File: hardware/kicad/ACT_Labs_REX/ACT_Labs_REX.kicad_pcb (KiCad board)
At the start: 2 copper layers, 138.8 x 120 mm, 40 parts, among them J1 PS1_Connector1, J2 JP1 Autofire, J3 JP3 Palanca Direccional, J4 JP4 Botones Frontales, J5 JP5 Botones laterales, J6 JP6 Autofire, SW1 SW_SPDT, SW10 SW_SPDT, SW2 SW_SPDT, SW3 SW_SPDT, SW4 SW_SPDT, SW5 SW_SPDT, SW6 SW_SPDT, SW7 SW_SPDT, SW8 SW_SPDT, SW9 SW_SPDT, U2 LD1117S33TR_SOT223

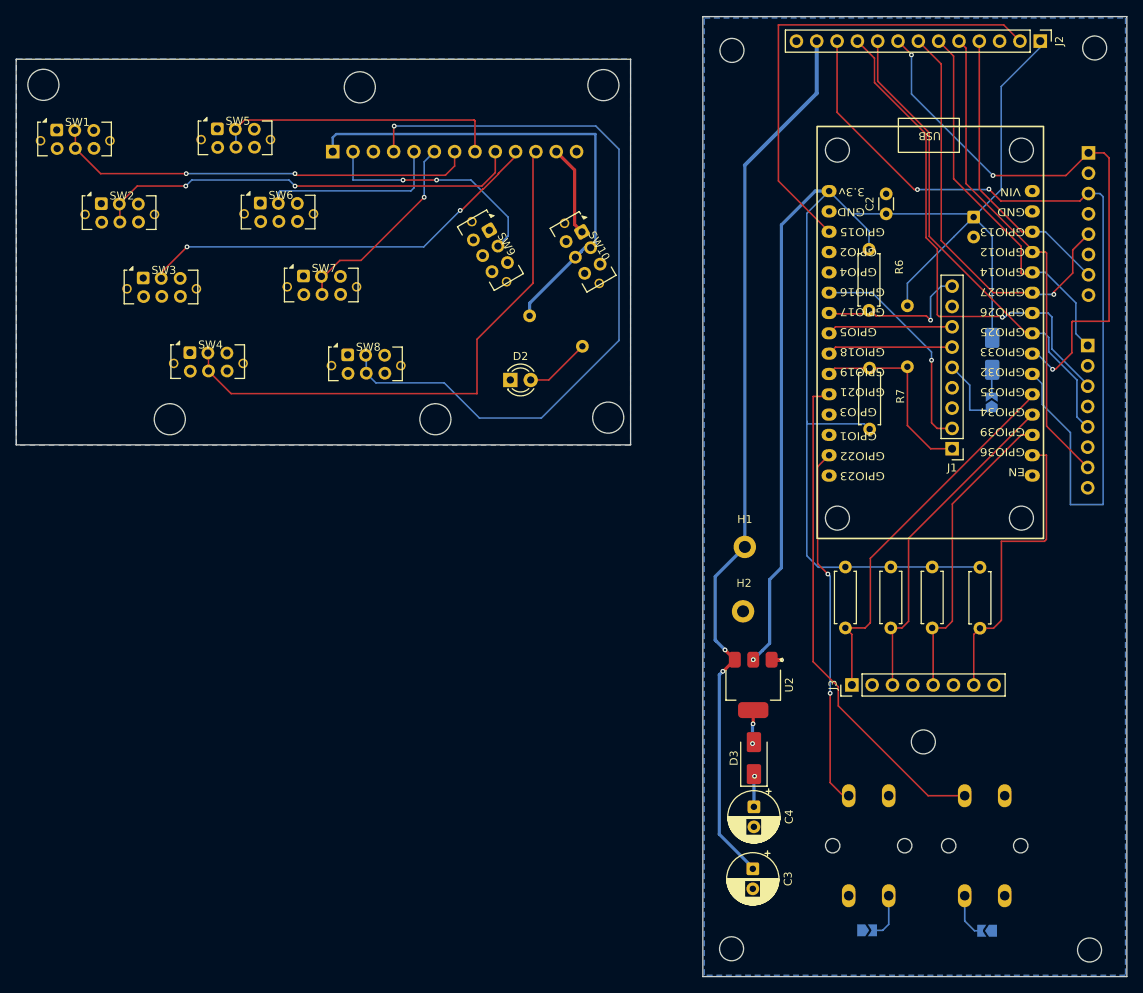
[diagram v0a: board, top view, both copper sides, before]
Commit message: hardware: update ACT Labs REX KiCad sources and gerbers
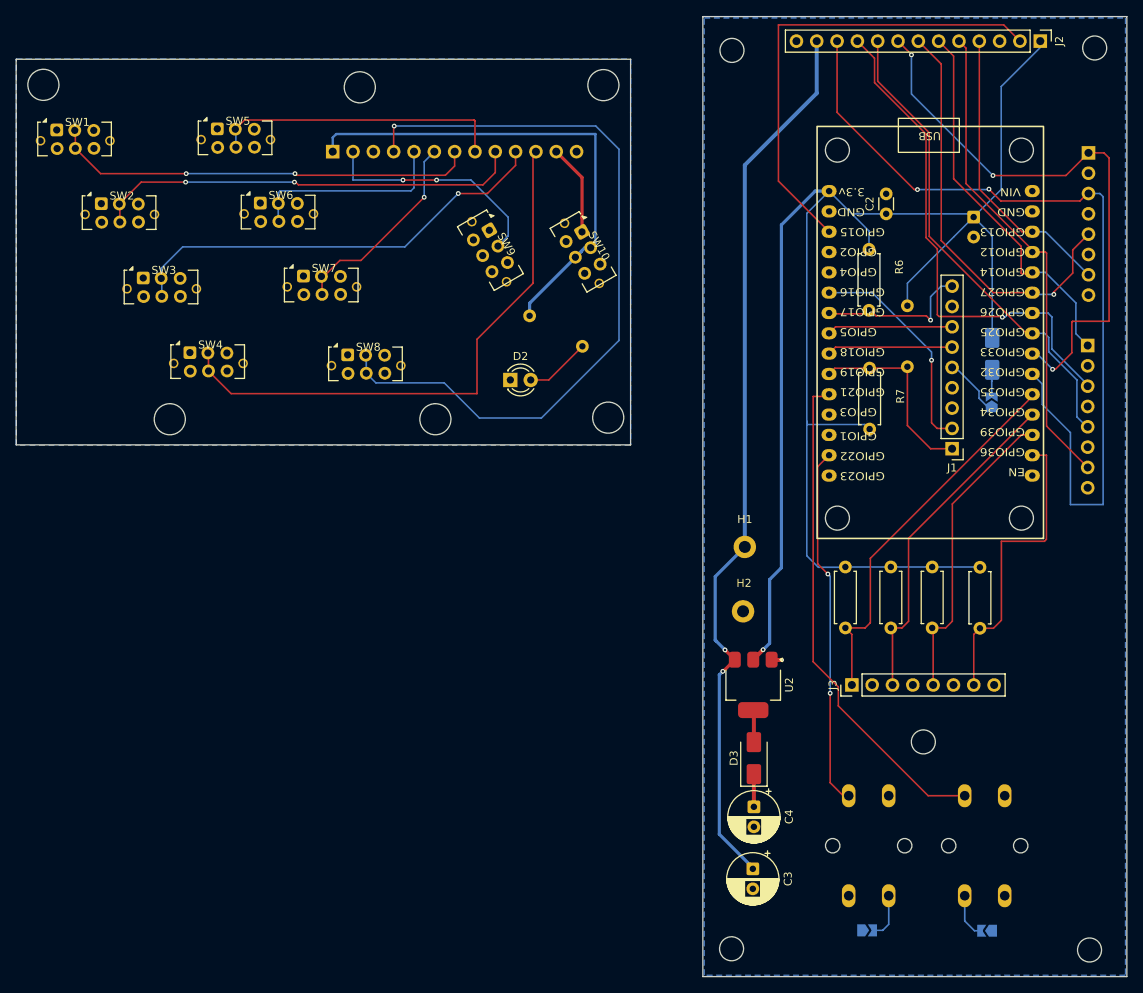
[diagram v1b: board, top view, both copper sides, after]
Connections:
- Select1 pad 1: //GND -> (no net)
- Select1 pad 2: //GND -> (no net)
- Start1 pad 2: //GND -> (no net)
- Start1 pad 3: //GND -> (no net)
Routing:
- net //AutoFire/AF_CIRCULO: track 51.8 -> 55.7 mm, vias 2 -> 1
- net //AutoFire/AF_CUADRADO: track 23.2 -> 25.5 mm
- net PS1_PIN5: track 12.7 -> 11.2 mm
- net VCC_3V3: track 292.2 -> 292.4 mm, vias 4 -> 1

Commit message: Add files via upload
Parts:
- removed R6, R7: 4.7kΩ, Resistor_THT:R_Axial_DIN0207_L6.3mm_D2.5mm_P7.62mm_Horizontal
- C1, D1, J4, J5, JP1, R1, R8: moved to F.Cu
- J2: moved to B.Cu
- moved H1 42.2 mm to (158.8, 140.7), turned to 90 degrees
- moved H2 38.2 mm to (158.7, 144.7), turned to 90 degrees
- moved D1 32.4 mm to (160.5, 69.6)
- moved JP1 31.9 mm to (160.9, 76.1)
- moved C1 27.8 mm to (163.2, 50.8), turned to 90 degrees
- moved C4 24.5 mm to (166.7, 106.9), turned to 90 degrees
- moved J1 23.7 mm to (164.1, 82.8)
- moved R1 20.7 mm to (168.0, 83.8), turned to 90 degrees
- moved C2 12.9 mm to (166.4, 56.2), turned to -90 degrees
- moved D3 11.8 mm to (164.7, 113.4), turned to -90 degrees
- moved C3 7.92 mm to (163.7, 131.0)
- moved U2 7.64 mm to (164.9, 123.2)
- moved R2 1.04 mm to (192.0, 101.1)
- moved R4 1.04 mm to (175.2, 101.1)
- moved R5 1.04 mm to (186.1, 101.1)
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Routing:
- net VCC_3V3: track 292.4 -> 239.9 mm, vias 1 -> 4
- net //PS1_DATA: track 24.7 -> 12.9 mm
- net //PS1_CMD: track 27.6 -> 19.0 mm
- net BATT_FROM_TP: track 124.0 -> 132.4 mm, vias 2 -> 1
- net //PS1_ACK: track 19.6 -> 12.1 mm, vias 1 -> 0
- net //PS1_ATT: track 15.7 -> 9.08 mm
- net //PS1_CLK: track 15.7 -> 9.42 mm
- net //AutoFire/AF_L2: track 70.3 -> 66.2 mm
- net //AutoFire/LED: track 8.21 -> 4.26 mm
- net //AF_L1: track 52.3 -> 49.9 mm
- net //JP3_ARRIBA: track 38.4 -> 36.8 mm
- net //JP3_ABAJO: track 47.8 -> 46.5 mm
- net //AutoFire/AF_TRIANGULO: track 25.5 -> 26.1 mm
- net //GND: track 1.89 -> 1.30 mm
- net //AF_TRIANGULO: track 47.7 -> 47.2 mm
